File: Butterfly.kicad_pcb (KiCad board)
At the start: 2 copper layers, 93.1 x 65.5 mm, 29 parts, among them J1 Conn_02x03_Odd_Even, J2 USB_A, J3 Conn_01x02, U1 ATTINY85-20PU

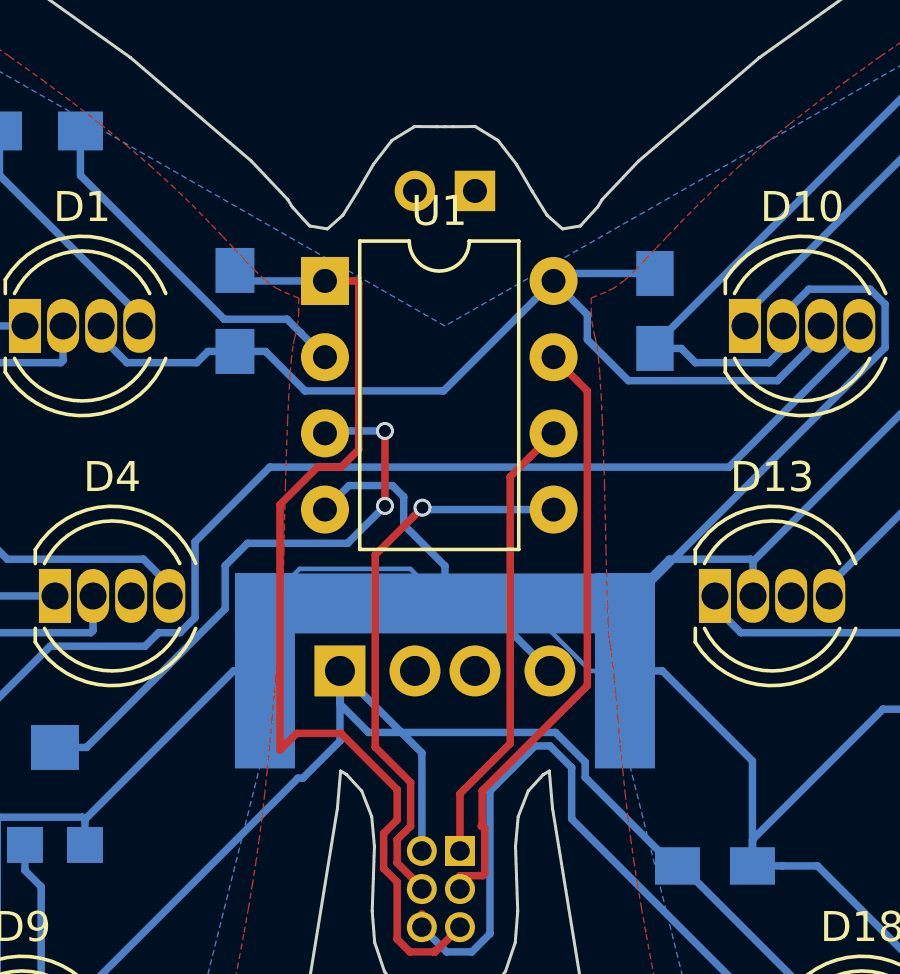
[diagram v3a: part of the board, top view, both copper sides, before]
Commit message: Center U1 exactly.
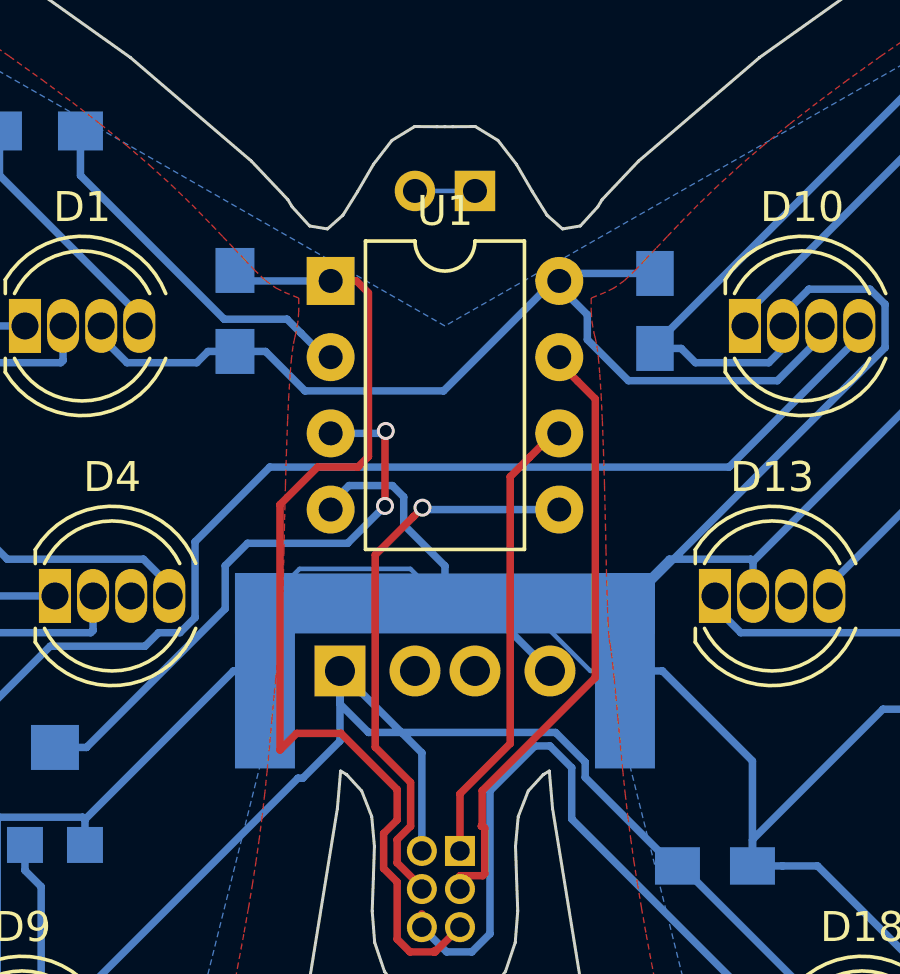
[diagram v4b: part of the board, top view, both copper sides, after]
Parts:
- moved U1 0.19 mm to (141.2, 93.5)
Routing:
- net Net-(J3-Pad1): track 0.00 -> 2.00 mm
- net Net-(J1-Pad5): track 34.4 -> 35.0 mm
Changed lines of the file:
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@@
   (general
     (links 76)
-    (no_connects 1)
-    (area 98.409153 69.322099 191.590847 150.013041)
+    (no_connects 0)
+    (area 98.409153 69.322099 191.590847 134.925641)
     (thickness 1.6)
     (drawings 182)
-    (tracks 344)
+    (tracks 346)
     (zones 0)
     (modules 29)
@@
   )
   (module Housings_DIP:DIP-8_W7.62mm (layer F.Cu)
-    (at 141 93.5)
+    (at 141.19 93.5)
     (descr "8-lead though-hole mounted DIP package, row spacing 7.62 mm (300 mils)")
     (tags "THT DIP DIL PDIP 2.54mm 7.62mm 300mil")
@@
   (segment (start 145.5 110.596509) (end 147.175001 108.921508) (width 0.25) (layer F.Cu) (net 22))
   (segment (start 145.5 112.5) (end 145.5 110.596509) (width 0.25) (layer F.Cu) (net 22))
+  (segment (start 145.5 113.77) (end 145.5 113.325001) (width 0.25) (layer F.Cu) (net 23))
+  (segment (start 149.419999 96.839999) (end 148.62 96.04) (width 0.25) (layer F.Cu) (net 23))
   (segment (start 145.5 113.325001) (end 146.260001 113.325001) (width 0.25) (layer F.Cu) (net 23))
+  (segment (start 146.260001 113.325001) (end 146.325001 113.260001) (width 0.25) (layer F.Cu) (net 23))
+  (segment (start 146.325001 113.260001) (end 146.325001 111.739999) (width 0.25) (layer F.Cu) (net 23))
+  (segment (start 146.325001 111.739999) (end 146.260001 111.674999) (width 0.25) (layer F.Cu) (net 23))
+  (segment (start 150.010351 97.430351) (end 149.419999 96.839999) (width 0.25) (layer F.Cu) (net 23))
+  (segment (start 146.260001 111.674999) (end 146.211411 111.674999) (width 0.25) (layer F.Cu) (net 23))
+  (segment (start 146.211411 111.674999) (end 146.241147 111.645263) (width 0.25) (layer F.Cu) (net 23))
   (segment (start 146.241147 111.645263) (end 146.241147 110.491772) (width 0.25) (layer F.Cu) (net 23))
-  (segment (start 146.325001 113.260001) (end 146.325001 111.739999) (width 0.25) (layer F.Cu) (net 23))
-  (segment (start 146.260001 113.325001) (end 146.325001 113.260001) (width 0.25) (layer F.Cu) (net 23))
-  (segment (start 149.745001 97.165001) (end 149.419999 96.839999) (width 0.25) (layer F.Cu) (net 23))
-  (segment (start 146.241147 110.491772) (end 149.745001 106.987918) (width 0.25) (layer F.Cu) (net 23))
-  (segment (start 146.211411 111.674999) (end 146.241147 111.645263) (width 0.25) (layer F.Cu) (net 23))
-  (segment (start 145.5 113.77) (end 145.5 113.325001) (width 0.25) (layer F.Cu) (net 23))
-  (segment (start 146.260001 111.674999) (end 146.211411 111.674999) (width 0.25) (layer F.Cu) (net 23))
-  (segment (start 146.325001 111.739999) (end 146.260001 111.674999) (width 0.25) (layer F.Cu) (net 23))
-  (segment (start 149.745001 106.987918) (end 149.745001 97.165001) (width 0.25) (layer F.Cu) (net 23))
-  (segment (start 149.419999 96.839999) (end 148.62 96.04) (width 0.25) (layer F.Cu) (net 23))
+  (segment (start 146.241147 110.491772) (end 150.010351 106.722568) (width 0.25) (layer F.Cu) (net 23))
+  (segment (start 150.010351 106.722568) (end 150.010351 97.430351) (width 0.25) (layer F.Cu) (net 23))
   (segment (start 148.62 101.12) (end 144.312201 101.12) (width 0.25) (layer B.Cu) (net 24))
   (segment (start 142.675001 102.632822) (end 143.950013 101.35781) (width 0.25) (layer F.Cu) (net 24))
@@
   (segment (start 143.950013 101.35781) (end 144.250012 101.057811) (width 0.25) (layer F.Cu) (net 24))
   (via (at 144.250012 101.057811) (size 0.6) (drill 0.4) (layers F.Cu B.Cu) (net 24))
+  (segment (start 145.5 115.04) (end 144.674999 115.865001) (width 0.25) (layer F.Cu) (net 25))
+  (segment (start 143.833999 115.865001) (end 143.404999 115.436001) (width 0.25) (layer F.Cu) (net 25))
   (segment (start 144.674999 115.816003) (end 144.626001 115.865001) (width 0.25) (layer F.Cu) (net 25))
   (segment (start 144.674999 115.865001) (end 144.674999 115.816003) (width 0.25) (layer F.Cu) (net 25))
-  (segment (start 145.5 115.04) (end 144.674999 115.865001) (width 0.25) (layer F.Cu) (net 25))
-  (segment (start 142.954988 111.917599) (end 143.404999 111.467588) (width 0.25) (layer F.Cu) (net 25))
+  (segment (start 144.626001 115.865001) (end 143.833999 115.865001) (width 0.25) (layer F.Cu) (net 25))
+  (segment (start 143.404999 115.436001) (end 143.404999 113.532412) (width 0.25) (layer F.Cu) (net 25))
+  (segment (start 143.404999 113.532412) (end 142.954988 113.082401) (width 0.25) (layer F.Cu) (net 25))
   (segment (start 142.954988 113.082401) (end 142.954988 111.917599) (width 0.25) (layer F.Cu) (net 25))
-  (segment (start 143.404999 113.532412) (end 142.954988 113.082401) (width 0.25) (layer F.Cu) (net 25))
-  (segment (start 143.404999 115.436001) (end 143.404999 113.532412) (width 0.25) (layer F.Cu) (net 25))
-  (segment (start 143.833999 115.865001) (end 143.404999 115.436001) (width 0.25) (layer F.Cu) (net 25))
-  (segment (start 144.626001 115.865001) (end 143.833999 115.865001) (width 0.25) (layer F.Cu) (net 25))
-  (segment (start 143.404999 110.451755) (end 141.53359 108.580346) (width 0.25) (layer F.Cu) (net 25))
-  (segment (start 143.404999 111.467588) (end 143.404999 110.451755) (width 0.25) (layer F.Cu) (net 25))
-  (segment (start 140.749997 99.705001) (end 141.540001 99.705001) (width 0.25) (layer F.Cu) (net 25))
   (segment (start 139.5 100.954998) (end 140.749997 99.705001) (width 0.25) (layer F.Cu) (net 25))
   (segment (start 139.5 109.135422) (end 139.5 100.954998) (width 0.25) (layer F.Cu) (net 25))
+  (segment (start 143.404999 110.451755) (end 141.53359 108.580346) (width 0.25) (layer F.Cu) (net 25))
+  (segment (start 140.749997 99.705001) (end 142.09891 99.705001) (width 0.25) (layer F.Cu) (net 25))
+  (segment (start 142.954988 111.917599) (end 143.404999 111.467588) (width 0.25) (layer F.Cu) (net 25))
+  (segment (start 143.404999 111.467588) (end 143.404999 110.451755) (width 0.25) (layer F.Cu) (net 25))
   (segment (start 140.055076 108.580346) (end 139.5 109.135422) (width 0.25) (layer F.Cu) (net 25))
   (segment (start 141.53359 108.580346) (end 140.055076 108.580346) (width 0.25) (layer F.Cu) (net 25))
-  (segment (start 141.540001 99.705001) (end 142.125001 99.120001) (width 0.25) (layer F.Cu) (net 25))
-  (segment (start 142.125001 99.120001) (end 142.125001 93.575001) (width 0.25) (layer F.Cu) (net 25))
-  (segment (start 142.125001 93.575001) (end 142.05 93.5) (width 0.25) (layer F.Cu) (net 25))
+  (segment (start 142.09891 99.705001) (end 142.449566 99.354345) (width 0.25) (layer F.Cu) (net 25))
+  (segment (start 142.449566 99.354345) (end 142.449566 93.899566) (width 0.25) (layer F.Cu) (net 25))
+  (segment (start 142.449566 93.899566) (end 142.05 93.5) (width 0.25) (layer F.Cu) (net 25))
   (segment (start 142.05 93.5) (end 141 93.5) (width 0.25) (layer F.Cu) (net 25))
   (segment (start 141 93.5) (end 138.35 93.5) (width 0.25) (layer B.Cu) (net 25))
@@
   (segment (start 139.734999 94.774999) (end 140.200001 95.240001) (width 0.25) (layer B.Cu) (net 28))
   (segment (start 140.200001 95.240001) (end 141 96.04) (width 0.25) (layer B.Cu) (net 28))
-  (segment (start 143 98.5) (end 141.08 98.5) (width 0.25) (layer B.Cu) (net 29))
-  (segment (start 141.08 98.5) (end 141 98.58) (width 0.25) (layer B.Cu) (net 29))
-  (segment (start 143 101) (end 143 98.5) (width 0.25) (layer F.Cu) (net 29))
-  (via (at 143 98.5) (size 0.6) (drill 0.4) (layers F.Cu B.Cu) (net 29))
+  (via (at 143.026976 98.5) (size 0.6) (drill 0.4) (layers F.Cu B.Cu) (net 29))
+  (segment (start 141 98.58) (end 142.946976 98.58) (width 0.25) (layer B.Cu) (net 29))
+  (segment (start 142.946976 98.58) (end 143.026976 98.5) (width 0.25) (layer B.Cu) (net 29))
+  (segment (start 143 101) (end 143 98.526976) (width 0.25) (layer F.Cu) (net 29))
+  (segment (start 143 98.526976) (end 143.026976 98.5) (width 0.25) (layer F.Cu) (net 29))
   (via (at 143 101) (size 0.6) (drill 0.4) (layers F.Cu B.Cu) (net 29))
   (segment (start 141.754999 102.245001) (end 143 101) (width 0.25) (layer B.Cu) (net 29))
@@
   (segment (start 137.674999 102.989999) (end 138.419997 102.245001) (width 0.25) (layer B.Cu) (net 29))
   (segment (start 138.419997 102.245001) (end 141.754999 102.245001) (width 0.25) (layer B.Cu) (net 29))
+  (segment (start 144 90.5) (end 146 90.5) (width 0.1524) (layer B.Cu) (net 30))
   (zone (net 1) (net_name +5V) (layer F.Cu) (hatch edge 0.508)
     (connect_pads (clearance 0.508))

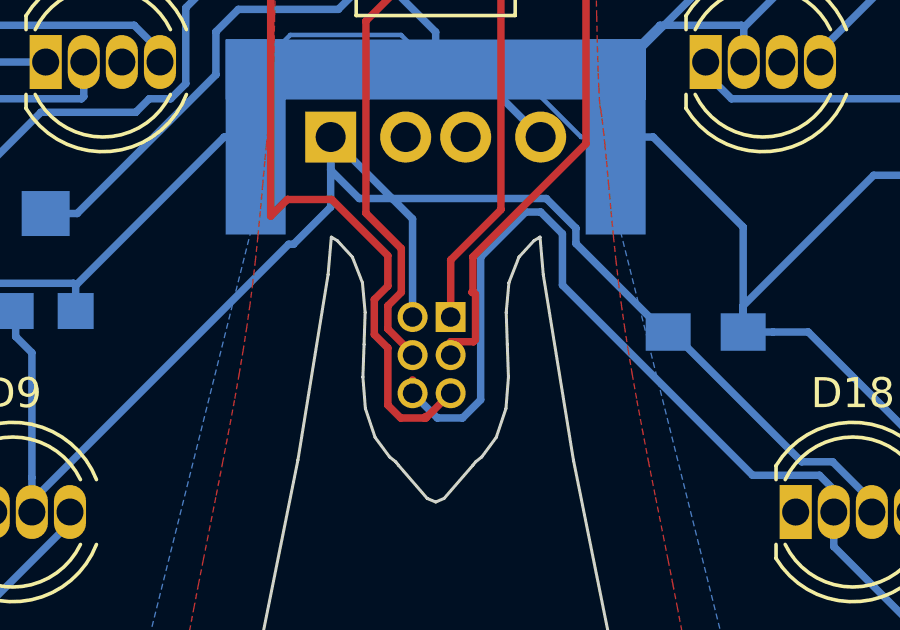
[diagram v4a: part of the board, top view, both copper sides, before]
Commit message: Center J1 exactly.
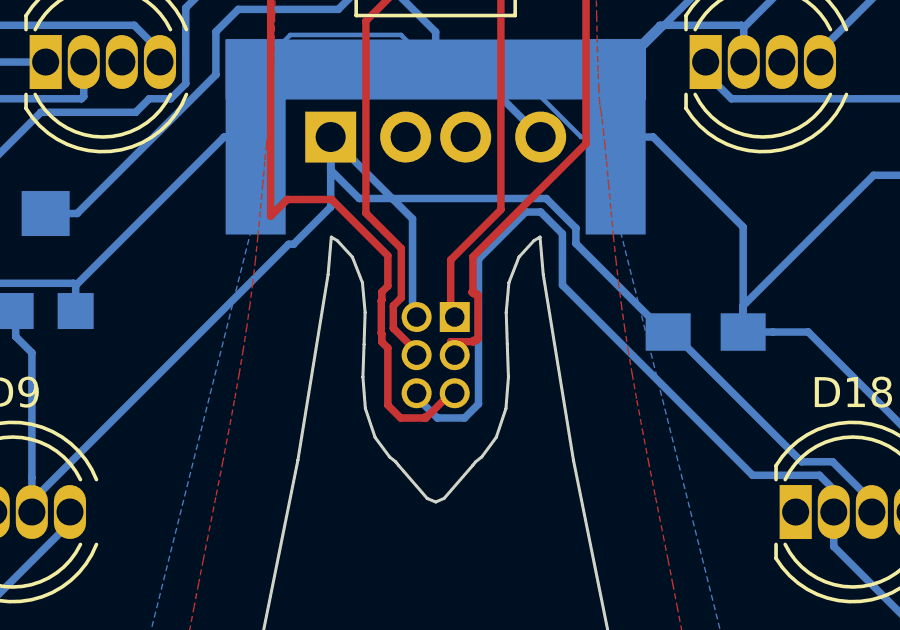
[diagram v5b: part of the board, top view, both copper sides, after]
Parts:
- moved J1 0.13 mm to (145.6, 112.5)

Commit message: Clean up a few tracks.
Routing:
- net Net-(J1-Pad5): track 34.8 -> 32.4 mm
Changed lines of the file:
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@@
     (pad_to_mask_clearance 0)
     (aux_axis_origin 0 0)
-    (visible_elements FFFEF37F)
+    (visible_elements FFFEF77F)
     (pcbplotparams
       (layerselection 0x00030_80000001)
@@
   (segment (start 145.5 112.5) (end 145.5 110.596509) (width 0.25) (layer F.Cu) (net 22))
   (segment (start 145.5 113.77) (end 145.5 113.325001) (width 0.25) (layer F.Cu) (net 23))
-  (segment (start 146.267479 111.722599) (end 146.267479 111.682477) (width 0.25) (layer F.Cu) (net 23))
+  (segment (start 146.267479 113.317523) (end 146.267479 113.277401) (width 0.25) (layer F.Cu) (net 23))
   (segment (start 146.260001 113.325001) (end 146.267479 113.317523) (width 0.25) (layer F.Cu) (net 23))
+  (segment (start 145.5 113.325001) (end 146.260001 113.325001) (width 0.25) (layer F.Cu) (net 23))
   (segment (start 146.267479 111.682477) (end 146.260001 111.674999) (width 0.25) (layer F.Cu) (net 23))
-  (segment (start 145.5 113.325001) (end 146.260001 113.325001) (width 0.25) (layer F.Cu) (net 23))
-  (segment (start 146.267479 113.317523) (end 146.267479 113.277401) (width 0.25) (layer F.Cu) (net 23))
+  (segment (start 146.267479 113.277401) (end 146.356921 113.277401) (width 0.25) (layer F.Cu) (net 23))
   (segment (start 146.356921 113.277401) (end 146.412401 113.221921) (width 0.25) (layer F.Cu) (net 23))
-  (segment (start 146.267479 113.277401) (end 146.356921 113.277401) (width 0.25) (layer F.Cu) (net 23))
-  (segment (start 146.260001 111.674999) (end 146.211411 111.674999) (width 0.25) (layer F.Cu) (net 23))
-  (segment (start 149.419999 96.839999) (end 148.62 96.04) (width 0.25) (layer F.Cu) (net 23))
-  (segment (start 146.211411 111.674999) (end 146.241147 111.645263) (width 0.25) (layer F.Cu) (net 23))
-  (segment (start 146.241147 111.645263) (end 146.241147 110.491772) (width 0.25) (layer F.Cu) (net 23))
   (segment (start 146.412401 113.221921) (end 146.412401 111.778079) (width 0.25) (layer F.Cu) (net 23))
   (segment (start 146.412401 111.778079) (end 146.356921 111.722599) (width 0.25) (layer F.Cu) (net 23))
   (segment (start 146.356921 111.722599) (end 146.267479 111.722599) (width 0.25) (layer F.Cu) (net 23))
-  (segment (start 146.241147 110.491772) (end 150.010351 106.722568) (width 0.25) (layer F.Cu) (net 23))
-  (segment (start 150.010351 106.722568) (end 150.010351 97.430351) (width 0.25) (layer F.Cu) (net 23))
-  (segment (start 150.010351 97.430351) (end 149.419999 96.839999) (width 0.25) (layer F.Cu) (net 23))
+  (segment (start 146.267479 111.722599) (end 146.267479 111.682477) (width 0.25) (layer F.Cu) (net 23))
+  (segment (start 146.241147 111.645263) (end 146.241147 110.491772) (width 0.25) (layer F.Cu) (net 23))
+  (segment (start 146.211411 111.674999) (end 146.241147 111.645263) (width 0.25) (layer F.Cu) (net 23))
+  (segment (start 146.260001 111.674999) (end 146.211411 111.674999) (width 0.25) (layer F.Cu) (net 23))
+  (segment (start 149.893146 106.839773) (end 149.893146 97.313146) (width 0.25) (layer F.Cu) (net 23))
+  (segment (start 146.241147 110.491772) (end 149.893146 106.839773) (width 0.25) (layer F.Cu) (net 23))
+  (segment (start 149.893146 97.313146) (end 149.419999 96.839999) (width 0.25) (layer F.Cu) (net 23))
+  (segment (start 149.419999 96.839999) (end 148.62 96.04) (width 0.25) (layer F.Cu) (net 23))
   (segment (start 143.950013 101.35781) (end 144.250012 101.057811) (width 0.25) (layer F.Cu) (net 24))
   (segment (start 143.587599 112.126847) (end 143.85501 111.859436) (width 0.25) (layer F.Cu) (net 24))
@@
   (segment (start 144.312201 101.12) (end 144.250012 101.057811) (width 0.25) (layer B.Cu) (net 24))
   (via (at 144.250012 101.057811) (size 0.6) (drill 0.4) (layers F.Cu B.Cu) (net 24))
-  (segment (start 140.055076 108.580346) (end 139.5 109.135422) (width 0.25) (layer F.Cu) (net 25))
+  (segment (start 145.5 115.04) (end 144.674999 115.865001) (width 0.25) (layer F.Cu) (net 25))
+  (segment (start 140.104893 100.350105) (end 140.749997 99.705001) (width 0.25) (layer F.Cu) (net 25))
+  (segment (start 142.09891 99.705001) (end 142.449566 99.354345) (width 0.25) (layer F.Cu) (net 25))
+  (segment (start 144.674999 115.865001) (end 144.674999 115.816003) (width 0.25) (layer F.Cu) (net 25))
+  (segment (start 144.626001 115.865001) (end 143.833999 115.865001) (width 0.25) (layer F.Cu) (net 25))
+  (segment (start 144.674999 115.816003) (end 144.626001 115.865001) (width 0.25) (layer F.Cu) (net 25))
+  (segment (start 143.404999 113.532412) (end 143.205743 113.333156) (width 0.25) (layer F.Cu) (net 25))
   (segment (start 143.404999 115.436001) (end 143.404999 113.532412) (width 0.25) (layer F.Cu) (net 25))
-  (segment (start 143.404999 113.532412) (end 143.205743 113.333156) (width 0.25) (layer F.Cu) (net 25))
-  (segment (start 145.5 115.04) (end 144.674999 115.865001) (width 0.25) (layer F.Cu) (net 25))
-  (segment (start 144.674999 115.865001) (end 144.674999 115.816003) (width 0.25) (layer F.Cu) (net 25))
-  (segment (start 144.674999 115.816003) (end 144.626001 115.865001) (width 0.25) (layer F.Cu) (net 25))
-  (segment (start 140.749997 99.705001) (end 142.09891 99.705001) (width 0.25) (layer F.Cu) (net 25))
-  (segment (start 144.626001 115.865001) (end 143.833999 115.865001) (width 0.25) (layer F.Cu) (net 25))
   (segment (start 143.833999 115.865001) (end 143.404999 115.436001) (width 0.25) (layer F.Cu) (net 25))
+  (segment (start 143.205743 113.333156) (end 143.205743 113.060392) (width 0.25) (layer F.Cu) (net 25))
+  (segment (start 143.185188 113.039837) (end 143.185188 111.960163) (width 0.25) (layer F.Cu) (net 25))
   (segment (start 143.205743 113.060392) (end 143.185188 113.039837) (width 0.25) (layer F.Cu) (net 25))
-  (segment (start 143.205743 113.333156) (end 143.205743 113.060392) (width 0.25) (layer F.Cu) (net 25))
   (segment (start 143.185188 111.960163) (end 143.205743 111.939608) (width 0.25) (layer F.Cu) (net 25))
-  (segment (start 143.185188 113.039837) (end 143.185188 111.960163) (width 0.25) (layer F.Cu) (net 25))
   (segment (start 143.205743 111.939608) (end 143.205743 111.666844) (width 0.25) (layer F.Cu) (net 25))
+  (segment (start 143.404999 110.451755) (end 141.53359 108.580346) (width 0.25) (layer F.Cu) (net 25))
   (segment (start 143.404999 111.467588) (end 143.404999 110.451755) (width 0.25) (layer F.Cu) (net 25))
   (segment (start 143.205743 111.666844) (end 143.404999 111.467588) (width 0.25) (layer F.Cu) (net 25))
-  (segment (start 143.404999 110.451755) (end 141.53359 108.580346) (width 0.25) (layer F.Cu) (net 25))
-  (segment (start 141.53359 108.580346) (end 140.055076 108.580346) (width 0.25) (layer F.Cu) (net 25))
+  (segment (start 140.749997 99.705001) (end 142.09891 99.705001) (width 0.25) (layer F.Cu) (net 25))
+  (segment (start 141.53359 108.580346) (end 141.425068 108.580346) (width 0.25) (layer F.Cu) (net 25))
+  (segment (start 141.425068 108.580346) (end 140.104893 107.260171) (width 0.25) (layer F.Cu) (net 25))
+  (segment (start 140.104893 107.260171) (end 140.104893 100.350105) (width 0.25) (layer F.Cu) (net 25))
+  (segment (start 142.449566 99.354345) (end 142.449566 93.899566) (width 0.25) (layer F.Cu) (net 25))
   (segment (start 142.449566 93.899566) (end 142.05 93.5) (width 0.25) (layer F.Cu) (net 25))
-  (segment (start 142.449566 99.354345) (end 142.449566 93.899566) (width 0.25) (layer F.Cu) (net 25))
-  (segment (start 139.5 109.135422) (end 139.5 100.954998) (width 0.25) (layer F.Cu) (net 25))
-  (segment (start 139.5 100.954998) (end 140.749997 99.705001) (width 0.25) (layer F.Cu) (net 25))
-  (segment (start 142.09891 99.705001) (end 142.449566 99.354345) (width 0.25) (layer F.Cu) (net 25))
   (segment (start 142.05 93.5) (end 141 93.5) (width 0.25) (layer F.Cu) (net 25))
   (segment (start 141 93.5) (end 138.35 93.5) (width 0.25) (layer B.Cu) (net 25))
